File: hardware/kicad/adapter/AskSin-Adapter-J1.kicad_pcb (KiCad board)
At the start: 2 copper layers, 65 x 12 mm, 4 parts, among them J1 Stapelbuchse 2x20 (kopfueber), J2 Stiftleiste 1x20 (gerade Pins)

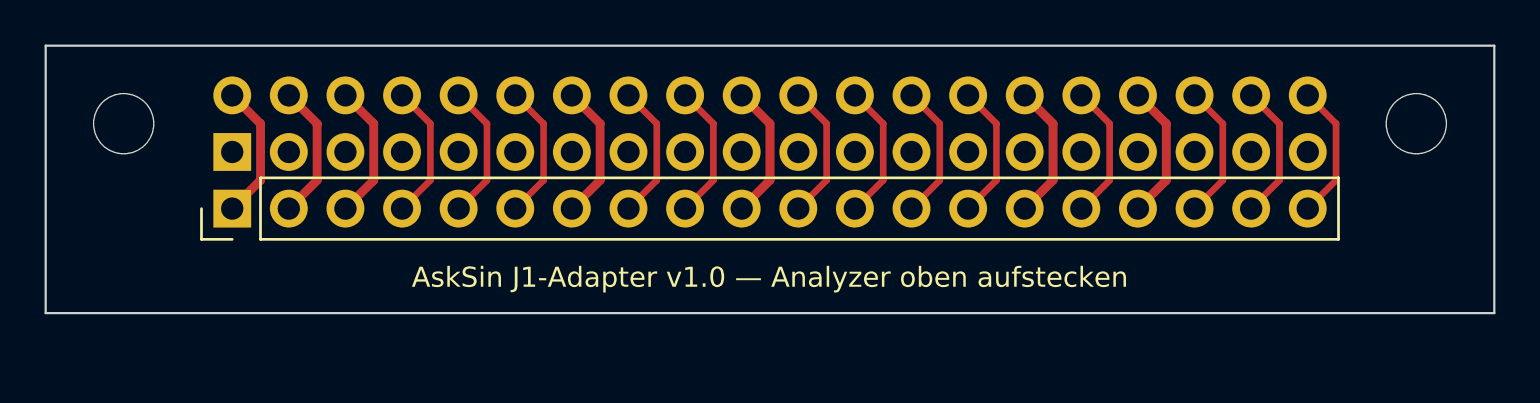
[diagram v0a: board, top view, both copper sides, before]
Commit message: J1-Adapter v1.1: drei einreihige Leisten statt Stapelbuchse 2x20
Die erste Fassung hätte nicht funktioniert: Bei einer 2x20-Stapelbuchse
ragen beide Reihen oben heraus — auch die bei 2,23 mm, für die die
Analyzer-Platine kein Loch hat. Sie hätte nicht aufsitzen können.

Jetzt konsequent nach dem Fehlerbild aufgebaut (nur die gerade Reihe
liegt falsch): J1 Stapelbuchse 1x20 auf der ungeraden Reihe (4,77) reicht
die Pins durch, J2 normale Buchsenleiste 1x20 auf der geraden Reihe
(2,23) bleibt oben bündig, J3 Stiftleiste 1x20 bei 7,31 nimmt deren
Signale auf. Courtyards auf den Leistenkörper zurückgeschnitten und
Leisten-Siebdruck entfernt, weil die drei Körper bauartbedingt
aneinanderstoßen.

DRC 0 Fehler / 0 Warnungen / 0 unverbunden, Pad-Positionen im Skript
gegen die HAT-Vorlage geprüft. Fertigungspaket neu gepackt.

Co-Authored-By: Claude Fable 5 <noreply@anthropic.com>
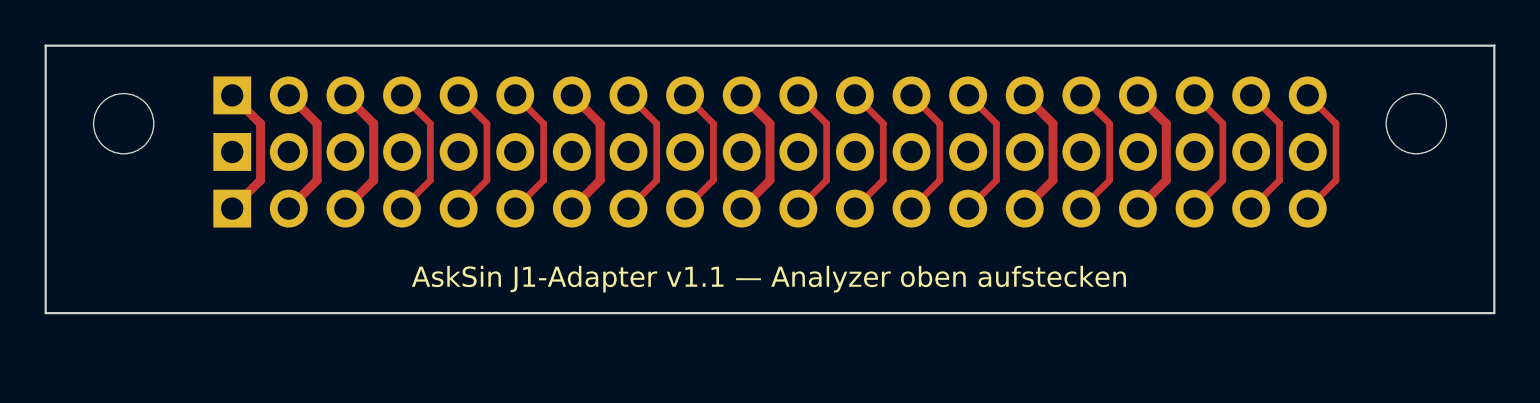
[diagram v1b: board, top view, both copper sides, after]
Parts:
- added J3: Stiftleiste 1x20 nach oben, PinHeader_1x20_P2.54mm_Vertical, F.Cu at (108.4, 67.3)
- J1: value Stapelbuchse 2x20 (kopfueber) -> Stapelbuchse 1x20 (Pins ragen oben durch); footprint PinSocket_2x20_P2.54mm_Vertical -> PinSocket_1x20_P2.54mm_Vertical; moved to F.Cu
- J2: value Stiftleiste 1x20 (gerade Pins) -> Buchsenleiste 1x20 (nicht stapelbar); footprint PinHeader_1x20_P2.54mm_Vertical -> PinSocket_1x20_P2.54mm_Vertical
- moved J2 5.08 mm to (108.4, 62.2)
- turned J1 to 90 degrees
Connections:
- J1 pad 10: P10 -> P19
- J1 pad 11: P11 -> P21
- J1 pad 12: P12 -> P23
- J1 pad 13: P13 -> P25
- J1 pad 14: P14 -> P27
- J1 pad 15: P15 -> P29
- J1 pad 16: P16 -> P31
- J1 pad 17: P17 -> P33
- J1 pad 18: P18 -> P35
- J1 pad 19: P19 -> P37
- J1 pad 2: P2 -> P3
- J1 pad 20: P20 -> P39
- J1 pad 3: P3 -> P5
- J1 pad 4: P4 -> P7
- J1 pad 5: P5 -> P9
- J1 pad 6: P6 -> P11
- J1 pad 7: P7 -> P13
- J1 pad 8: P8 -> P15
- J1 pad 9: P9 -> P17
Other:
- board text added: "AskSin J1-Adapter v1.1 — Analyzer oben aufstecken"
- board text removed: "AskSin J1-Adapter v1.0 — Analyzer oben aufstecken"

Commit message: J1-Adapter neu aufgebaut, Platine auf Hardware v0.2.0
**Adapter:** Die bisherige Fassung war unbrauchbar — sie setzte auf eine
Stapelbuchse, deren durchgereichte Pins mit den Stiften der zweiten
Leiste in der Höhe hätten zusammenpassen müssen. Tun sie nicht, die
Platine hätte nie aufgesessen.

Neuer Aufbau mit zwei gewöhnlichen Standardteilen: unten eine
Buchsenleiste 2x20 in exakter Pi-Geometrie (Reihen 2,23/4,77), oben eine
Stiftleiste 2x20 um 2,54 mm nach hinten versetzt (Reihen 7,31/9,85) —
genau dort erwartet die fehlerhafte Platine ihre Reihen. Jeder Pin geht
1:1 durch; ungerade Bahnen oben, gerade unten an den Pads vorbei.

Die Netze werden im Erzeuger **nach gemessener Pad-Position** vergeben
statt nach Pad-Nummer — die Verwechslung, die zum Platinenfehler geführt
hat, ist damit ausgeschlossen. verify_adapter.py prüft das fertige
Layout unabhängig gegen die offizielle KiCad-Vorlage RaspberryPi-HAT und
gegen den gefertigten Stand aus Tag hardware-v0.0.1: beide Steckbilder
decken sich mit genau einem Versatz über alle 40 Pins.
Preis: 2,54 mm Versatz nach hinten und rund 10 mm Bauhöhe.

**Platine:** Versionssprung 0.1.0 → 0.2.0, damit die neue Bauform nicht
mit der fehlerhaften Charge verwechselt wird — die Nummer steht im
Bestückungsdruck. Doku, Fertigungspaket und die 3D-Renderings im
Handbuch (Oberseite, Unterseite, Schrägansicht, Layout) auf den neuen
T-förmigen Umriss neu erzeugt.

Co-Authored-By: Claude Fable 5 <noreply@anthropic.com>
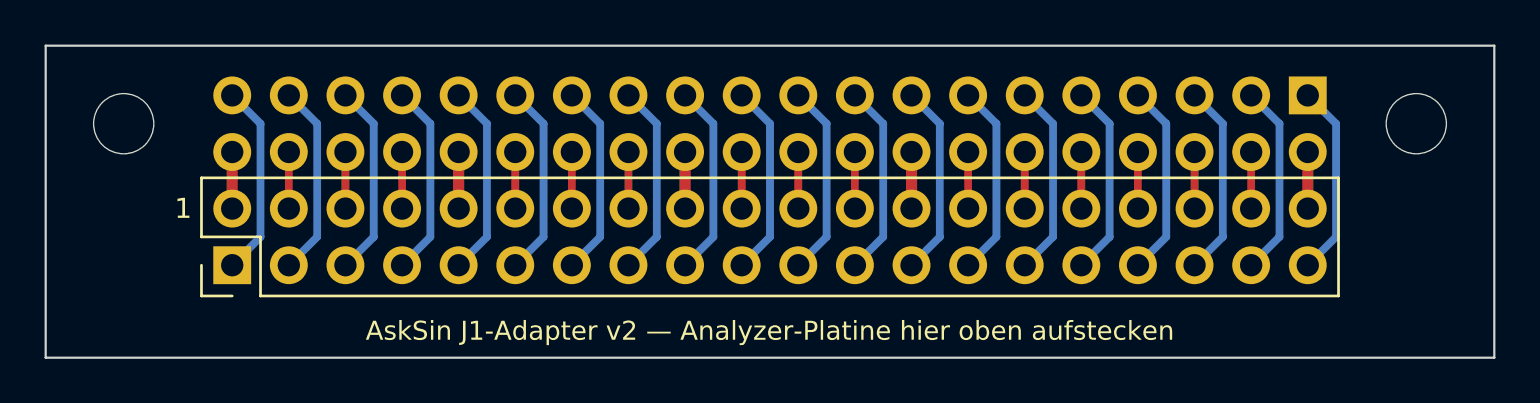
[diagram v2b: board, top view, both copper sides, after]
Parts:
- removed J3: Stiftleiste 1x20 nach oben, PinHeader_1x20_P2.54mm_Vertical
- J1: value Stapelbuchse 1x20 (Pins ragen oben durch) -> Buchsenleiste 2x20 (unten, zum PoE-HAT); footprint PinSocket_1x20_P2.54mm_Vertical -> PinSocket_2x20_P2.54mm_Vertical; moved to B.Cu
- J2: value Buchsenleiste 1x20 (nicht stapelbar) -> Stiftleiste 2x20 (oben, zur Platine); footprint PinSocket_1x20_P2.54mm_Vertical -> PinHeader_2x20_P2.54mm_Vertical
- moved J1 48.3 mm to (156.6, 62.2)
- moved J2 7.62 mm to (108.4, 69.8)
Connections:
- J1 pad 1: P1 -> P40
- J1 pad 10: P19 -> P31
- J1 pad 11: P21 -> P30
- J1 pad 12: P23 -> P29
- J1 pad 13: P25 -> P28
- J1 pad 15: P29 -> P26
- J1 pad 16: P31 -> P25
- J1 pad 17: P33 -> P24
- J1 pad 18: P35 -> P23
- J1 pad 19: P37 -> P22
- J1 pad 2: P3 -> P39
- J1 pad 20: P39 -> P21
- J1 pad 3: P5 -> P38
- J1 pad 4: P7 -> P37
- J1 pad 5: P9 -> P36
- J1 pad 6: P11 -> P35
- J1 pad 7: P13 -> P34
- J1 pad 8: P15 -> P33
- J1 pad 9: P17 -> P32
- J2 pad 10: P20 -> P9
- J2 pad 11: P22 -> P12
- J2 pad 12: P24 -> P11
- J2 pad 13: P26 -> P14
- J2 pad 14: P28 -> P13
- J2 pad 15: P30 -> P16
- J2 pad 16: P32 -> P15
- J2 pad 17: P34 -> P18
- J2 pad 18: P36 -> P17
- J2 pad 19: P38 -> P20
- J2 pad 2: P4 -> P1
- J2 pad 20: P40 -> P19
- J2 pad 3: P6 -> P4
- J2 pad 4: P8 -> P3
- J2 pad 5: P10 -> P6
- J2 pad 6: P12 -> P5
- J2 pad 7: P14 -> P8
- J2 pad 8: P16 -> P7
- J2 pad 9: P18 -> P10
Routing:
- net P8: track 6.13 -> 8.67 mm
- net P9: track 0.00 -> 2.54 mm
- net P7: track 0.00 -> 2.54 mm
- net P5: track 0.00 -> 2.54 mm
- net P39: track 0.00 -> 2.54 mm
- net P37: track 0.00 -> 2.54 mm
- net P35: track 0.00 -> 2.54 mm
- net P33: track 0.00 -> 2.54 mm
- net P31: track 0.00 -> 2.54 mm
- net P3: track 0.00 -> 2.54 mm
- net P29: track 0.00 -> 2.54 mm
- net P27: track 0.00 -> 2.54 mm
- net P25: track 0.00 -> 2.54 mm
- net P23: track 0.00 -> 2.54 mm
- net P21: track 0.00 -> 2.54 mm
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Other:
- board size 65 x 12 mm -> 65 x 14 mm
- board text added: "1"
- board text added: "AskSin J1-Adapter v2 — Analyzer-Platine hier oben aufstecken"
- board text added: "Diese Seite auf den PoE-HAT"
- board text removed: "AskSin J1-Adapter v1.1 — Analyzer oben aufstecken"
- board text removed: "Pi-Header unten"
